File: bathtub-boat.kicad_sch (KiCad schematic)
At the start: 25 parts, among them J1 I2C, J2 SPI, J3 I2C, J4 DS18B20, J5 1WireTRS, SW1 MODE, SW2 RESET, SW3 POWER, SW4 A, U1 esp-01m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

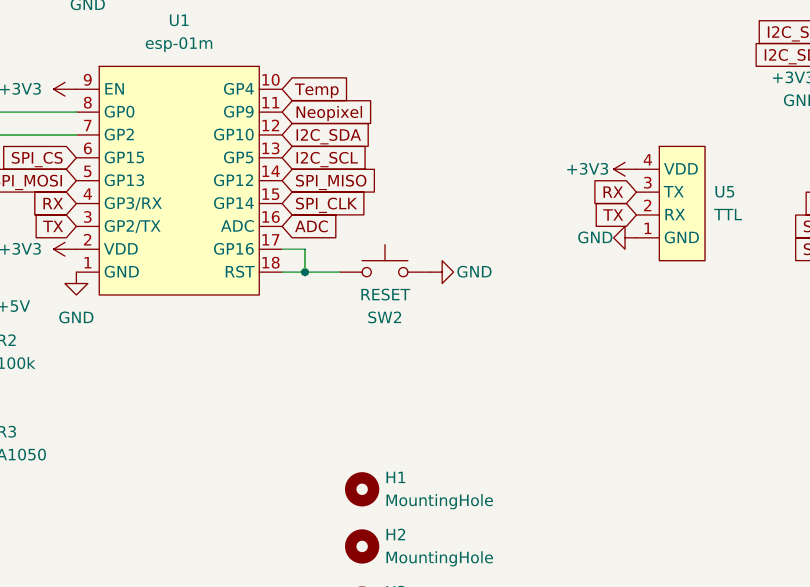
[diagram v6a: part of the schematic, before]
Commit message: Add solder jumper and testpoint for IO16
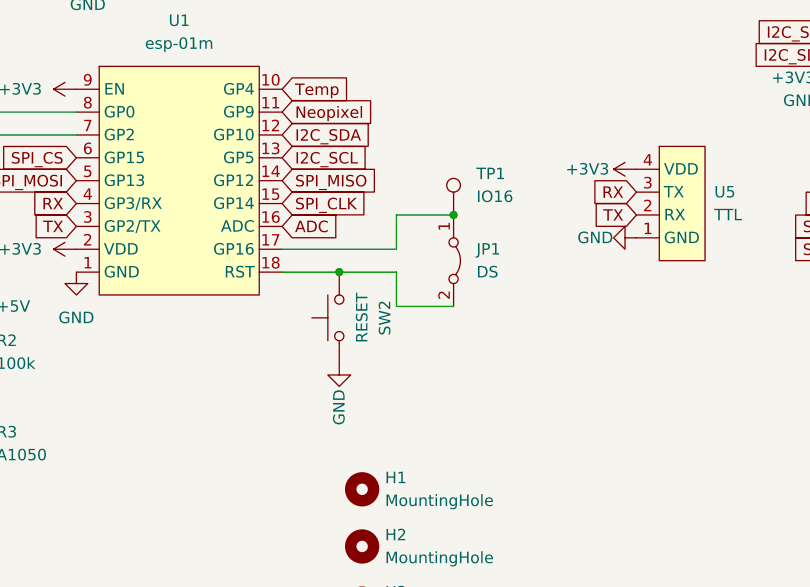
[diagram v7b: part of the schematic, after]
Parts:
- added JP1: DS, Jumper:SolderJumper-2_P1.3mm_Bridged_RoundedPad1.0x1.5mm, symbol Jumper:Jumper_2_Bridged
- added TP1: IO16, TestPoint:TestPoint_Pad_D1.0mm, symbol Connector:TestPoint
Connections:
- net at SW2.2, U1.18 (RST): now also JP1.2 (B); no longer U1.17 (GP16)
- new net: JP1.1 (A), TP1.1, U1.17 (GP16)
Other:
- moved on the sheet: SW2
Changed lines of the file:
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@@
   (junction (at 154.94 67.31) (diameter 0) (color 0 0 0 0)
   )
-  (junction (at 171.45 109.22) (diameter 0) (color 0 0 0 0)
+  (junction (at 187.96 102.87) (diameter 0) (color 0 0 0 0)
   )
   (junction (at 134.62 123.19) (diameter 0) (color 0 0 0 0)
   )
   (junction (at 82.55 63.5) (diameter 0) (color 0 0 0 0)
+  )
+  (junction (at 175.26 109.22) (diameter 0) (color 0 0 0 0)
   )
   (junction (at 139.7 67.31) (diameter 0) (color 0 0 0 0)
@@
     (stroke (width 0) (type default))
   )
-  (wire (pts (xy 171.45 106.68) (xy 171.45 109.22))
-    (stroke (width 0) (type default))
-  )
   (wire (pts (xy 226.06 58.42) (xy 227.33 58.42))
     (stroke (width 0) (type default))
@@
     (stroke (width 0) (type default))
   )
-  (wire (pts (xy 171.45 109.22) (xy 175.26 109.22))
-    (stroke (width 0) (type default))
-  )
   (wire (pts (xy 68.58 71.12) (xy 82.55 71.12))
     (stroke (width 0) (type default))
@@
     (stroke (width 0) (type default))
   )
-  (wire (pts (xy 168.91 106.68) (xy 171.45 106.68))
-    (stroke (width 0) (type default))
-  )
   (wire (pts (xy 82.55 59.69) (xy 97.79 59.69))
     (stroke (width 0) (type default))
@@
     (stroke (width 0) (type default))
   )
+  (wire (pts (xy 175.26 109.22) (xy 181.61 109.22))
+    (stroke (width 0) (type default))
+  )
   (wire (pts (xy 130.81 123.19) (xy 134.62 123.19))
     (stroke (width 0) (type default))
   )
+  (wire (pts (xy 181.61 113.03) (xy 187.96 113.03))
+    (stroke (width 0) (type default))
+  )
+  (wire (pts (xy 181.61 109.22) (xy 181.61 113.03))
+    (stroke (width 0) (type default))
+  )
+  (wire (pts (xy 181.61 102.87) (xy 181.61 106.68))
+    (stroke (width 0) (type default))
+  )
+  (wire (pts (xy 168.91 106.68) (xy 181.61 106.68))
+    (stroke (width 0) (type default))
+  )
   (wire (pts (xy 226.06 54.61) (xy 226.06 58.42))
     (stroke (width 0) (type default))
   )
-  (wire (pts (xy 168.91 109.22) (xy 171.45 109.22))
+  (wire (pts (xy 168.91 109.22) (xy 175.26 109.22))
+    (stroke (width 0) (type default))
+  )
+  (wire (pts (xy 187.96 102.87) (xy 181.61 102.87))
     (stroke (width 0) (type default))
   )
@@
     )
   )
+  (symbol (lib_id "Jumper:Jumper_2_Bridged") (at 187.96 107.95 270) (unit 1)
+    (in_bom yes) (on_board yes) (dnp no) (fields_autoplaced)
+    (property "Reference" "JP1" (at 190.5 106.68 90)
+      (effects (font (size 1.27 1.27)) (justify left))
+    )
+    (property "Value" "DS" (at 190.5 109.22 90)
+      (effects (font (size 1.27 1.27)) (justify left))
+    )
+    (property "Footprint" "Jumper:SolderJumper-2_P1.3mm_Bridged_RoundedPad1.0x1.5mm" (at 187.96 107.95 0)
+      (effects (font (size 1.27 1.27)) hide)
+    )
+    (property "Datasheet" "~" (at 187.96 107.95 0)
+      (effects (font (size 1.27 1.27)) hide)
+    )
+    (pin "1")
+    (pin "2")
+    (instances
+      (project "bathtub-boat"
+        (path "/d50afe49-2e50-4685-b8a6-e43e950be1b7"
+          (reference "JP1") (unit 1)
+        )
+      )
+    )
+  )
   (symbol (lib_id "Mechanical:MountingHole") (at 177.8 133.35 0) (unit 1)
     (in_bom yes) (on_board yes) (dnp no) (fields_autoplaced)
@@
     )
   )
-  (symbol (lib_id "Switch:SW_Push") (at 180.34 109.22 0) (mirror y) (unit 1)
+  (symbol (lib_id "Switch:SW_Push") (at 175.26 114.3 90) (unit 1)
     (in_bom yes) (on_board yes) (dnp no)
     (property "Reference" "SW2" (at 180.34 114.3 0)
       (effects (font (size 1.27 1.27)))
     )
-    (property "Value" "RESET" (at 180.34 111.76 0)
-      (effects (font (size 1.27 1.27)))
-    )
-    (property "Footprint" "pts636:pts636" (at 180.34 104.14 0)
-      (effects (font (size 1.27 1.27)) hide)
-    )
-    (property "Datasheet" "~" (at 180.34 104.14 0)
+    (property "Value" "RESET" (at 177.8 114.3 0)
+      (effects (font (size 1.27 1.27)))
+    )
+    (property "Footprint" "pts636:pts636" (at 170.18 114.3 0)
+      (effects (font (size 1.27 1.27)) hide)
+    )
+    (property "Datasheet" "~" (at 170.18 114.3 0)
       (effects (font (size 1.27 1.27)) hide)
     )
@@
     )
   )
-  (symbol (lib_id "power:GND") (at 185.42 109.22 90) (mirror x) (unit 1)
+  (symbol (lib_id "power:GND") (at 175.26 119.38 0) (mirror y) (unit 1)
     (in_bom yes) (on_board yes) (dnp no)
-    (property "Reference" "#PWR0115" (at 191.77 109.22 0)
-      (effects (font (size 1.27 1.27)) hide)
-    )
-    (property "Value" "GND" (at 192.278 109.22 90)
-      (effects (font (size 1.27 1.27)) (justify left))
-    )
-    (property "Footprint" "" (at 185.42 109.22 0)
-      (effects (font (size 1.27 1.27)) hide)
-    )
-    (property "Datasheet" "" (at 185.42 109.22 0)
+    (property "Reference" "#PWR0115" (at 175.26 125.73 0)
+      (effects (font (size 1.27 1.27)) hide)
+    )
+    (property "Value" "GND" (at 175.26 126.238 90)
+      (effects (font (size 1.27 1.27)) (justify left))
+    )
+    (property "Footprint" "" (at 175.26 119.38 0)
+      (effects (font (size 1.27 1.27)) hide)
+    )
+    (property "Datasheet" "" (at 175.26 119.38 0)
       (effects (font (size 1.27 1.27)) hide)
     )
@@
         )
       )
+    )
+  )
+  (symbol (lib_id "Connector:TestPoint") (at 187.96 102.87 0) (unit 1)
+    (in_bom yes) (on_board yes) (dnp no) (fields_autoplaced)
+    (property "Reference" "TP1" (at 190.5 98.298 0)
+      (effects (font (size 1.27 1.27)) (justify left))
+    )
+    (property "Value" "IO16" (at 190.5 100.838 0)
+      (effects (font (size 1.27 1.27)) (justify left))
+    )
+    (property "Footprint" "TestPoint:TestPoint_Pad_D1.0mm" (at 193.04 102.87 0)
+      (effects (font (size 1.27 1.27)) hide)
+    )
+    (property "Datasheet" "~" (at 193.04 102.87 0)
+      (effects (font (size 1.27 1.27)) hide)
+    )
+    (pin "1")
+    (instances
+      (project "bathtub-boat"
+        (path "/d50afe49-2e50-4685-b8a6-e43e950be1b7"
+          (reference "TP1") (unit 1)
+        )
+      )
